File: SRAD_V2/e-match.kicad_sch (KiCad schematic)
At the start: 28 parts, among them IC1 NCV81071BZR2G, IC2 NCV81071BZR2G, J2 691210910002, J3 691210910002, J4 691210910002, J5 691210910002, Q1 AOSP36326C, Q2 AOSP36326C, Q3 FDC8878, Q4 FDC8878, U3 TMCS1108A2UQDR

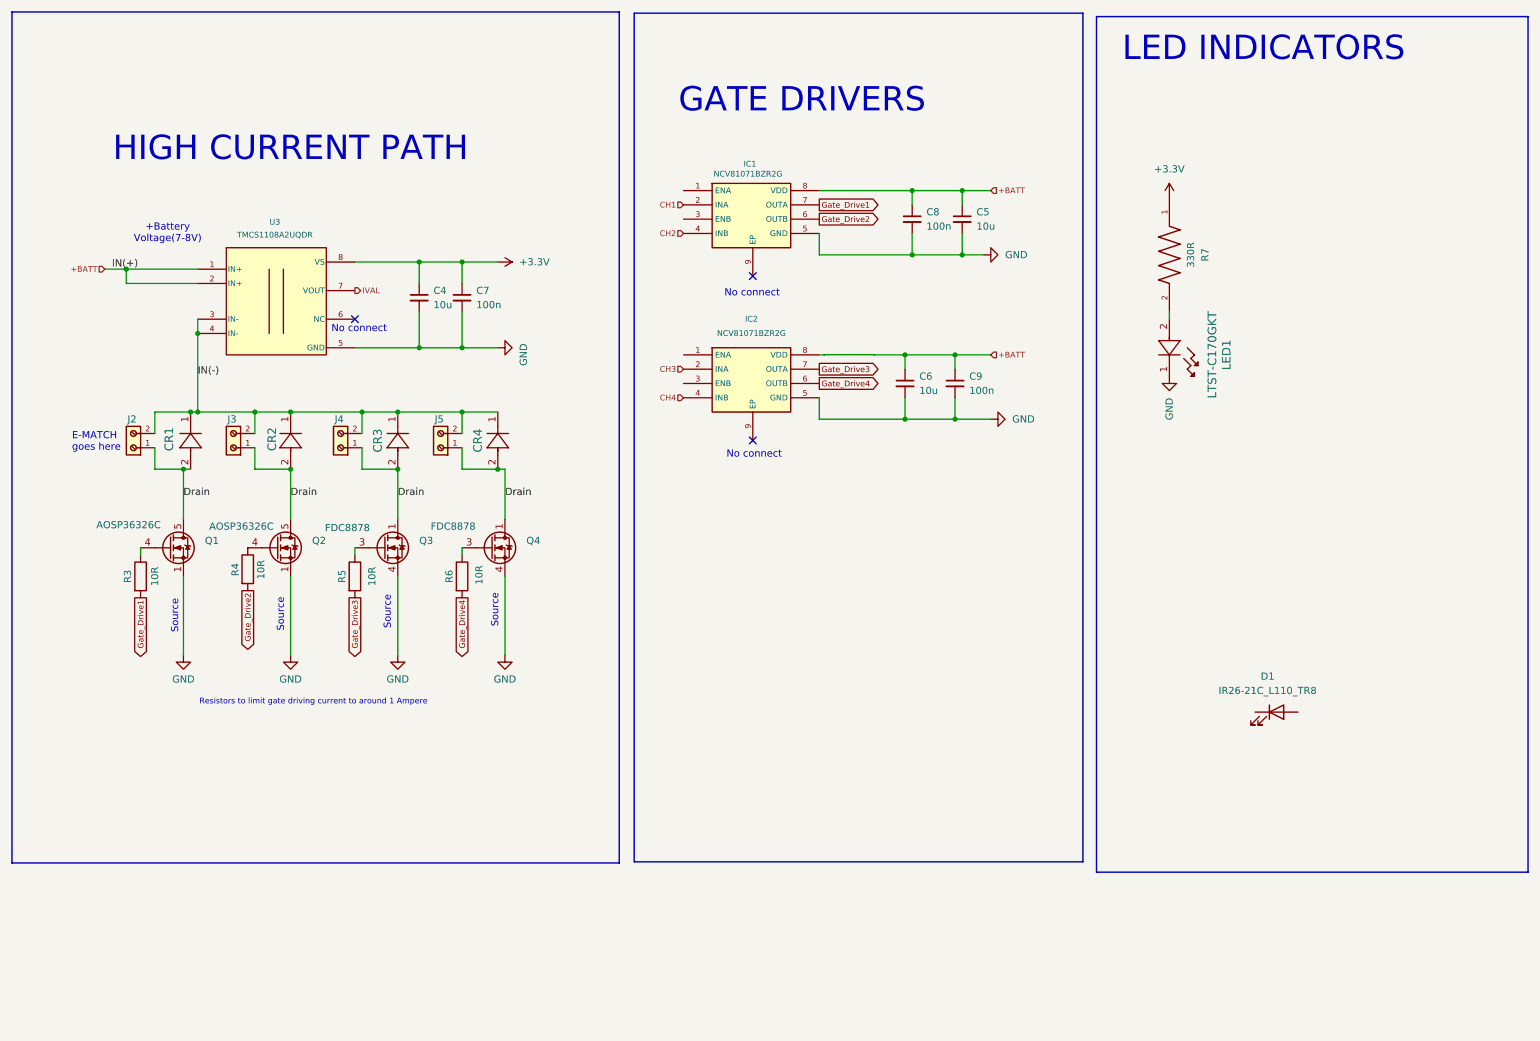
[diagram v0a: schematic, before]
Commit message: Added an input LC filter
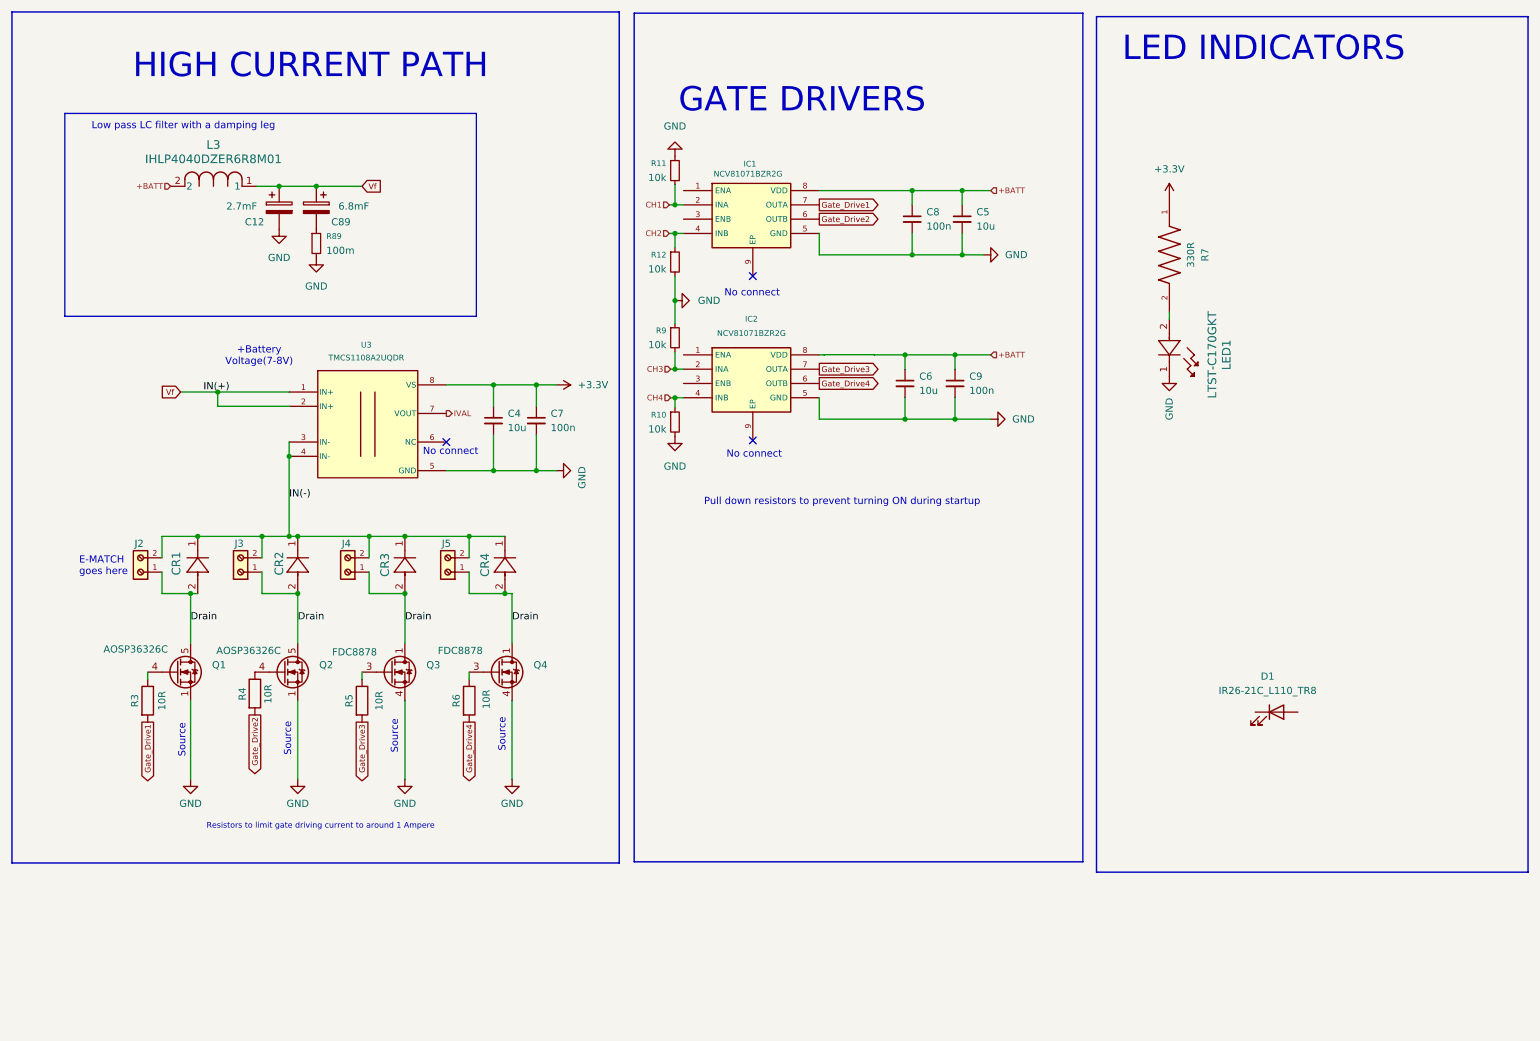
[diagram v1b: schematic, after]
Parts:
- added C12: 2.7mF, Capacitor_THT:CP_Radial_D10.0mm_P5.00mm, symbol Device:C_Polarized
- added C89: 6.8mF, Capacitor_THT:CP_Radial_D16.0mm_P7.50mm, symbol Device:C_Polarized
- added L3: IHLP4040DZER6R8M01, 6.8uH Inductor:IND_IHLP-4040DZ_VIS, symbol 6.8uH Inductor:IHLP4040DZER6R8M01
- added R10, R11, R12, R9: 10k, symbol Device:R_Small
- added R89: 100m, symbol Device:R_Small
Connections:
- net +BATT: now also L3.2; no longer U3.1 (IN+), U3.2 (IN+)
- net CH1: now also R11.2
- net CH2: now also R12.1
- net CH3: now also R9.2
- net CH4: now also R10.1
- net GND: now also C12.2, R10.2, R11.1, R12.2, R89.2, R9.1
- new net: C89.2, R89.1
- new net Vf: C12.1, C89.1, L3.1, U3.1 (IN+), U3.2 (IN+)
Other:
- note added: "Low pass LC filter with a damping leg"
- note added: "Pull down resistors to prevent turning ON during startup"
- moved on the sheet: C4, C7, CR1, CR2, CR3, CR4, J2, J3, J4, J5, Q1, Q2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

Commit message: fiddling with the layout
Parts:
- removed D1: IR26-21C_L110_TR8, LED_SMD:LED_1206_3216Metric, symbol LED:IR26-21C_L110_TR8
- added F1, F2, F3, F4: Fuse_Small, Fuse:Fuse_1206_3216Metric_Pad1.42x1.75mm_HandSolder, symbol Device:Fuse_Small
- added Q5: NTMFS5C673NT1G, NTMFS5C673NT1G-2:TRANS_NTMFS5C673NT1G, symbol NTMFS5C673NT1G:NTMFS5C673NT1G
- R89: footprint (none) -> Resistor_SMD:R_1206_3216Metric
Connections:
- removed net Drain: CR1.2, CR2.2, CR3.2, CR4.2, J2.1, J3.1, J4.1, J5.1, Q1.5 (D), Q1.6 (D), Q1.7 (D), Q1.8 (D), Q2.5 (D), Q2.6 (D), Q2.7 (D), Q2.8 (D), Q3.1 (D), Q3.2 (D), Q3.5 (D), Q3.6 (D), Q4.1 (D), Q4.2 (D), Q4.5 (D), Q4.6 (D)
- new net: CR2.2, F2.2, J3.1
- new net: CR3.2, F3.2, J4.1
- new net: CR1.2, F1.2, J2.1
- new net: CR4.2, F4.2, J5.1
- new net Drain1: F1.1, Q1.5 (D), Q1.6 (D), Q1.7 (D), Q1.8 (D)
- new net Drain2: F2.1, Q2.5 (D), Q2.6 (D), Q2.7 (D), Q2.8 (D)
- new net Drain3: F3.1, Q3.1 (D), Q3.2 (D), Q3.5 (D), Q3.6 (D)
- new net Drain4: F4.1, Q4.1 (D), Q4.2 (D), Q4.5 (D), Q4.6 (D)
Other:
- moved on the sheet: CR4, J5, Q1, Q2, Q3, Q4, R3, R4, R5, R6

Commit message: Reorganising the PCB layout
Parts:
- removed Q3, Q4: FDC8878, Package_TO_SOT_SMD:SOT-23-6, symbol Transistor_FET:RQ6E080AJ
- added Q4: NTMFS5C673NT1G, NTMFS5C673NT1G-2:TRANS_NTMFS5C673NT1G, symbol NTMFS5C673NT1G:NTMFS5C673NT1G
- renumbered Q5 to Q3
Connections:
- net Drain3: now also Q3.5
- net Drain4: now also Q4.5
- net GND: now also Q3.1, Q3.2, Q3.3, Q4.1, Q4.2, Q4.3
- net at R6.1: now also Q4.4
- net at R5.1: now also Q3.4
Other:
- moved on the sheet: Q3, R5, R6
